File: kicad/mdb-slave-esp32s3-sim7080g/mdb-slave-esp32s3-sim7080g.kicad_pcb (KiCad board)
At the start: 2 copper layers, 65 x 40 mm, 82 parts, among them J1 USB_C_Receptacle_USB2.0_16P, J2 JAE_SIM_Card_SF72S006, J3 Conn_01x03_Pin, J4 Conn_Coaxial, J5 Conn_Coaxial, J6 MDB_Connector, J7 Conn_01x03_Pin, J8 Conn_01x04_Pin, Q1 MMBT3904, Q2 MMBT3904, Q3 MMBT3904, Q4 MMBT3904, Q5 MMBT3904, Q6 MMBT3904, Q7 MMBT3904, SW1 SW_Push, U1 ESP32-S3FH4R2, U2 SIM7080G, U3 LM2594HVM-3.3, U4 TLP785, U5 TLP785, Y1 Crystal_GND24

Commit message: Routing
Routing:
- net Net-(U1-LNA_IN/RF): track 11.7 -> 0.00 mm
- net /gnss_ant: track 7.28 -> 1.70 mm
- net /rf_ant: track 4.62 -> 1.60 mm
- net Net-(J4-In): track 4.12 -> 1.70 mm
- net /io4: track 25.2 -> 25.8 mm

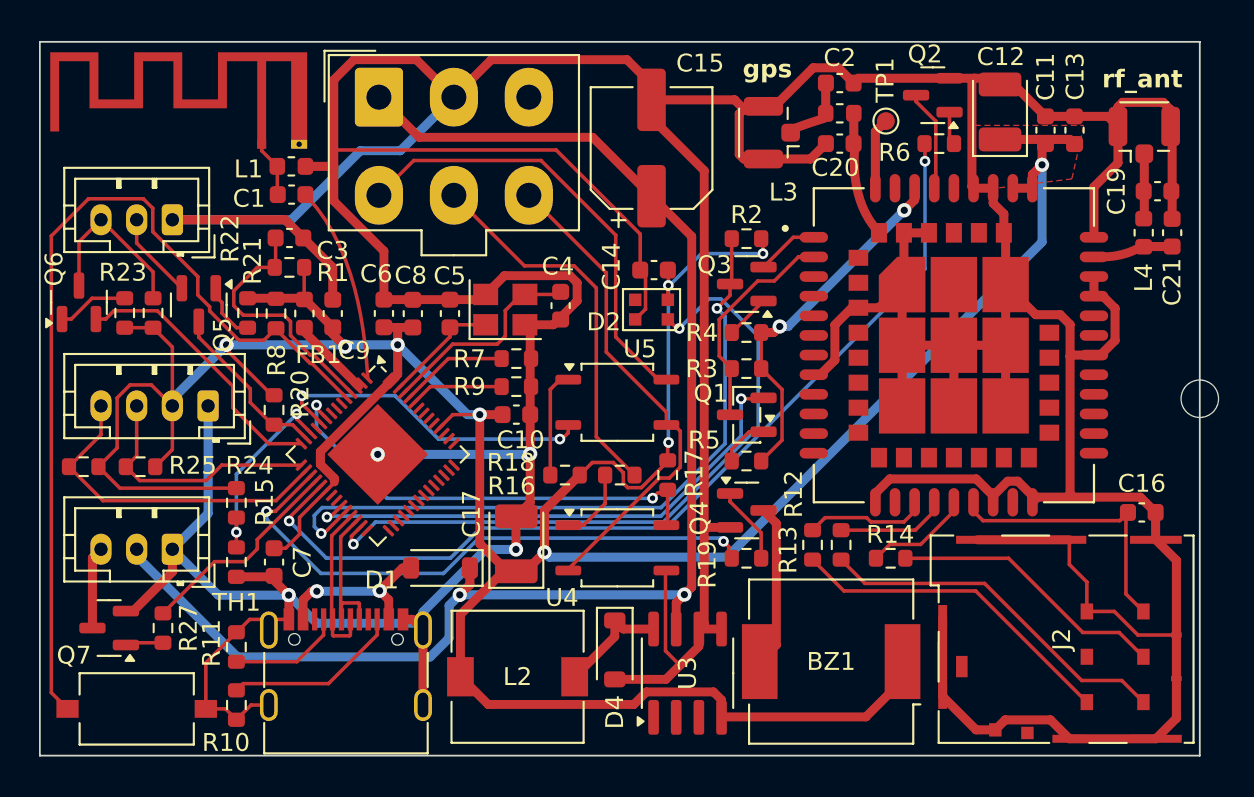
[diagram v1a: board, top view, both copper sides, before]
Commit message: Updating PCBway rules
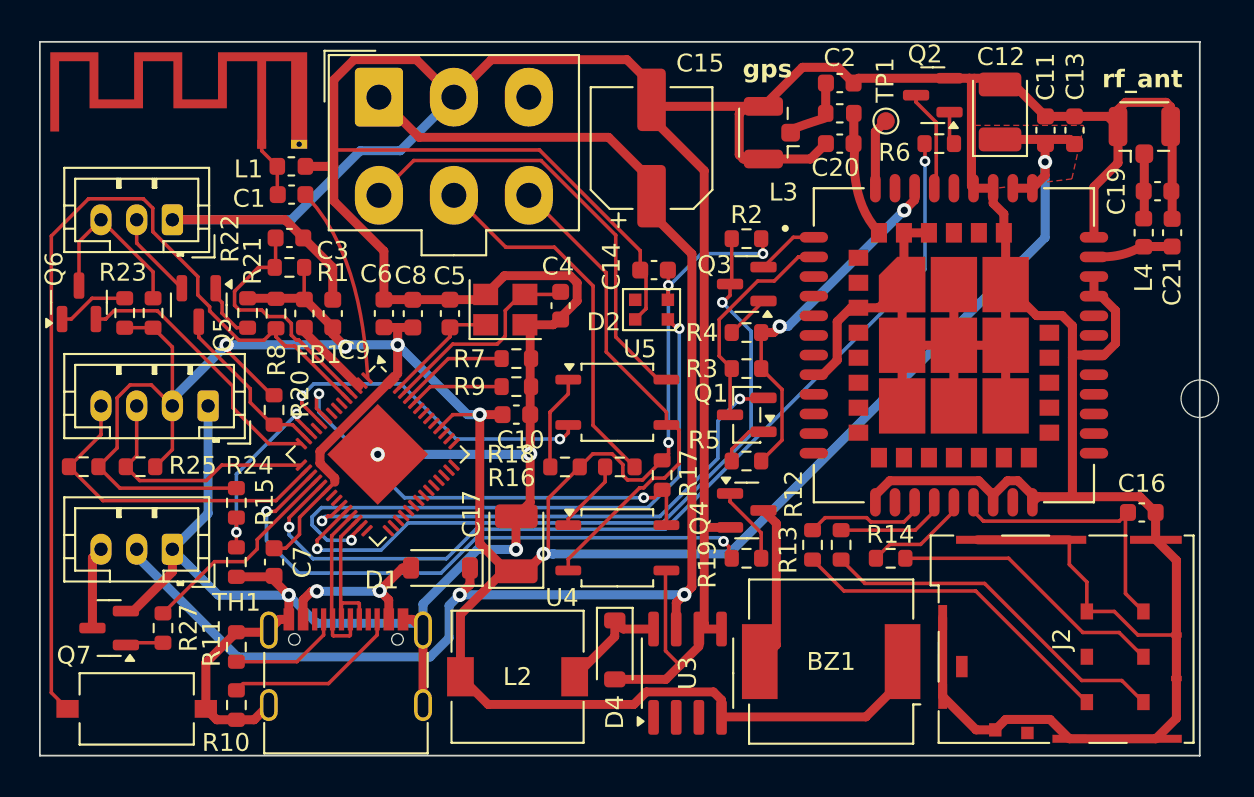
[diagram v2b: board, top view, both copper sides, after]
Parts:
- moved R16 0.46 mm to (201.0, 106.9)
- moved R18 0.46 mm to (197.9, 106.9)
- moved R17 0.31 mm to (203.4, 107.4)
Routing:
- net /io21: track 38.6 -> 34.7 mm
- net /io18: track 39.8 -> 41.7 mm
- net GND: track 427.7 -> 428.5 mm
- net /io17: track 29.5 -> 30.3 mm
- net /io12: track 32.7 -> 33.4 mm
- net Net-(R18-Pad2): track 6.03 -> 5.32 mm
- net /io5: track 18.5 -> 19.1 mm
- net /vin: track 80.8 -> 81.3 mm
- net /io14: track 53.0 -> 53.5 mm

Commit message: PCBway rules
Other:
- board text added: "d_rx"
- board text added: "d_tx"
- board text added: "gnd"
- board text added: "pulse"
- board text added: "scl"
- board text added: "sda"
- board text added: "vin"
- board text removed: "DEX"
- board text removed: "D_RX"
- board text removed: "D_TX"
- board text removed: "GND"
- board text removed: "PULSE"
- board text removed: "SCL"
- board text removed: "SDA"
- board text removed: "VIN"
- board text removed: "_i2c"
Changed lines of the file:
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@@
 		(tags "resistor")
 		(property "Reference" "R18"
-			(at 3.0375 0.7075 0)
+			(at 2.9375 0.16 0)
 			(layer "F.SilkS")
 			(effects
@@
 		(tags "capacitor")
 		(property "Reference" "C10"
-			(at 0.239166 1.42 0)
+			(at -0.250834 1.41 0)
 			(layer "F.SilkS")
 			(effects
@@
 		(tags "resistor")
 		(property "Reference" "R16"
-			(at 6.07 -0.6125 0)
+			(at 5.93 -1.16 0)
 			(layer "F.SilkS")
 			(effects
@@
 			)
 			(scale
-				(xyz 2 1 1.7)
+				(xyz 1.8 1 1.7)
 			)
 			(rotate
@@
 		)
 	)
-	(gr_text "PULSE"
-		(at 170.67 105.28 90)
+	(gr_text "pulse"
+		(at 172.589 105.75619 90)
 		(layer "B.SilkS" knockout)
 		(effects
@@
 		)
 	)
-	(gr_text "PULSE"
-		(at 172.53 105.28 90)
-		(layer "B.SilkS" knockout)
-		(effects
-			(font
-				(size 1 1)
-				(thickness 0.2)
-				(bold yes)
-			)
-			(justify left bottom mirror)
-		)
-	)
-	(gr_text "_i2c"
-		(at 170.67 98.78 90)
-		(layer "B.SilkS" knockout)
-		(effects
-			(font
-				(size 1 1)
-				(thickness 0.2)
-				(bold yes)
-			)
-			(justify left bottom mirror)
-		)
-	)
-	(gr_text "VIN"
-		(at 174.53 107.613334 90)
+	(gr_text "vin"
+		(at 174.589 107.613334 90)
 		(layer "B.SilkS" knockout)
 		(effects
@@
 	)
 	(gr_text "3v3"
-		(at 176.589 99.160952 90)
+		(at 176.589 98.970476 90)
 		(layer "B.SilkS" knockout)
 		(effects
@@
 		)
 	)
-	(gr_text "SDA"
+	(gr_text "sda"
 		(at 174.589 99.018095 90)
 		(layer "B.SilkS" knockout)
@@
 		)
 	)
-	(gr_text "GND"
-		(at 176.53 106.946667 90)
+	(gr_text "gnd"
+		(at 176.589 107.041905 90)
 		(layer "B.SilkS" knockout)
 		(effects
@@
 		)
 	)
-	(gr_text "GND"
-		(at 178.57 98.78 90)
+	(gr_text "gnd"
+		(at 178.589 98.922857 90)
 		(layer "B.SilkS" knockout)
 		(effects
@@
 		)
 	)
-	(gr_text "DEX"
-		(at 170.67 88.472381 90)
-		(layer "B.SilkS" knockout)
-		(effects
-			(font
-				(size 1 1)
-				(thickness 0.2)
-				(bold yes)
-			)
-			(justify left bottom mirror)
-		)
-	)
-	(gr_text "SCL"
-		(at 172.589 99.065714 90)
+	(gr_text "scl"
+		(at 172.589 99.446666 90)
 		(layer "B.SilkS" knockout)
 		(effects
@@
 		)
 	)
-	(gr_text "D_TX"
-		(at 172.589 87.853333 90)
+	(gr_text "d_tx"
+		(at 172.589 87.948571 90)
 		(layer "B.SilkS" knockout)
 		(effects
@@
 		)
 	)
-	(gr_text "D_RX"
-		(at 174.589 87.615238 90)
+	(gr_text "d_rx"
+		(at 174.589 87.900952 90)
 		(layer "B.SilkS" knockout)
 		(effects
@@
 		)
 	)
-	(gr_text "GND"
-		(at 176.5 88.281905 90)
+	(gr_text "gnd"
+		(at 176.589 88.281905 90)
 		(layer "B.SilkS" knockout)
 		(effects
@@
 	)
 	(zone
-		(net 3)
-		(net_name "GND")
+		(net 10)
+		(net_name "/mdb_master_transmit")
 		(layer "F.Cu")
 		(name "$teardrop_padvia$")
 		(hatch none 0.1)
-		(priority 30002)
+		(priority 30003)
 		(attr
 			(teardrop
@@
 		(polygon
 			(pts
-				(xy 190.080049 84.216496) (xy 189.726496 84.570049) (xy 190.35 86.254213) (xy 191.700707 86.190707)
-				(xy 191.485911 84.561698)
+				(xy 193.424885 93.558569) (xy 193.568569 93.414885) (xy 193.05 91.625786) (xy 191.699293 91.689293)
+				(xy 191.914088 93.318301)
 			)
 		)
 	)
 	(zone
-		(net 3)
-		(net_name "GND")
+		(net 11)
+		(net_name "/mdb_communications_common")
 		(layer "F.Cu")
 		(name "$teardrop_padvia$")
 		(hatch none 0.1)
-		(priority 30001)
+		(priority 30004)
 		(attr
 			(teardrop
@@
 		(polygon
 			(pts
-				(xy 193.673504 84.570049) (xy 193.319951 84.216496) (xy 191.914088 84.561698) (xy 191.699293 86.190707)
-				(xy 193.05 86.254214)
+				(xy 197.626017 93.557438) (xy 197.767438 93.416017) (xy 197.25 91.625786) (xy 195.899293 91.689293)
+				(xy 196.114087 93.318301)
 			)
 		)
 	)
 	(zone
-		(net 12)
-		(net_name "/mdb_master_receive")
+		(net 7)
+		(net_name "/vin")
 		(layer "F.Cu")
 		(name "$teardrop_padvia$")
 		(hatch none 0.1)
-		(priority 30005)
+		(priority 30000)
 		(attr
 			(teardrop
@@
 		(polygon
 			(pts
-				(xy 189.367438 89.963983) (xy 189.226017 89.822562) (xy 187.714088 90.061698) (xy 187.499293 91.690707)
-				(xy 188.85 91.754214)
+				(xy 189.38033 88.423883) (xy 189.733883 88.07033) (xy 188.849999 86.125786) (xy 187.499293 86.189293)
+				(xy 187.735785 87.839999)
 			)
 		)
 	)
 	(zone
-		(net 11)
-		(net_name "/mdb_communications_common")
+		(net 3)
+		(net_name "GND")
 		(layer "F.Cu")
 		(name "$teardrop_padvia$")
 		(hatch none 0.1)
-		(priority 30004)
+		(priority 30002)
 		(attr
 			(teardrop
@@
 		(polygon
 			(pts
-				(xy 197.626017 93.557438) (xy 197.767438 93.416017) (xy 197.25 91.625786) (xy 195.899293 91.689293)
-				(xy 196.114087 93.318301)
+				(xy 190.080049 84.216496) (xy 189.726496 84.570049) (xy 190.35 86.254213) (xy 191.700707 86.190707)
+				(xy 191.485911 84.561698)
 			)
 		)
 	)
 	(zone
-		(net 10)
-		(net_name "/mdb_master_transmit")
+		(net 12)
+		(net_name "/mdb_master_receive")
 		(layer "F.Cu")
 		(name "$teardrop_padvia$")
 		(hatch none 0.1)
-		(priority 30003)
+		(priority 30005)
 		(attr
 			(teardrop
@@
 		(polygon
 			(pts
-				(xy 193.424885 93.558569) (xy 193.568569 93.414885) (xy 193.05 91.625786) (xy 191.699293 91.689293)
-				(xy 191.914088 93.318301)
+				(xy 189.367438 89.963983) (xy 189.226017 89.822562) (xy 187.714088 90.061698) (xy 187.499293 91.690707)
+				(xy 188.85 91.754214)
 			)
 		)
 	)
 	(zone
-		(net 7)
-		(net_name "/vin")
+		(net 3)
+		(net_name "GND")
 		(layer "F.Cu")
 		(name "$teardrop_padvia$")
 		(hatch none 0.1)
-		(priority 30000)
+		(priority 30001)
 		(attr
 			(teardrop
@@
 		(polygon
 			(pts
-				(xy 189.38033 88.423883) (xy 189.733883 88.07033) (xy 188.849999 86.125786) (xy 187.499293 86.189293)
-				(xy 187.735785 87.839999)
+				(xy 193.673504 84.570049) (xy 193.319951 84.216496) (xy 191.914088 84.561698) (xy 191.699293 86.190707)
+				(xy 193.05 86.254214)
 			)
 		)

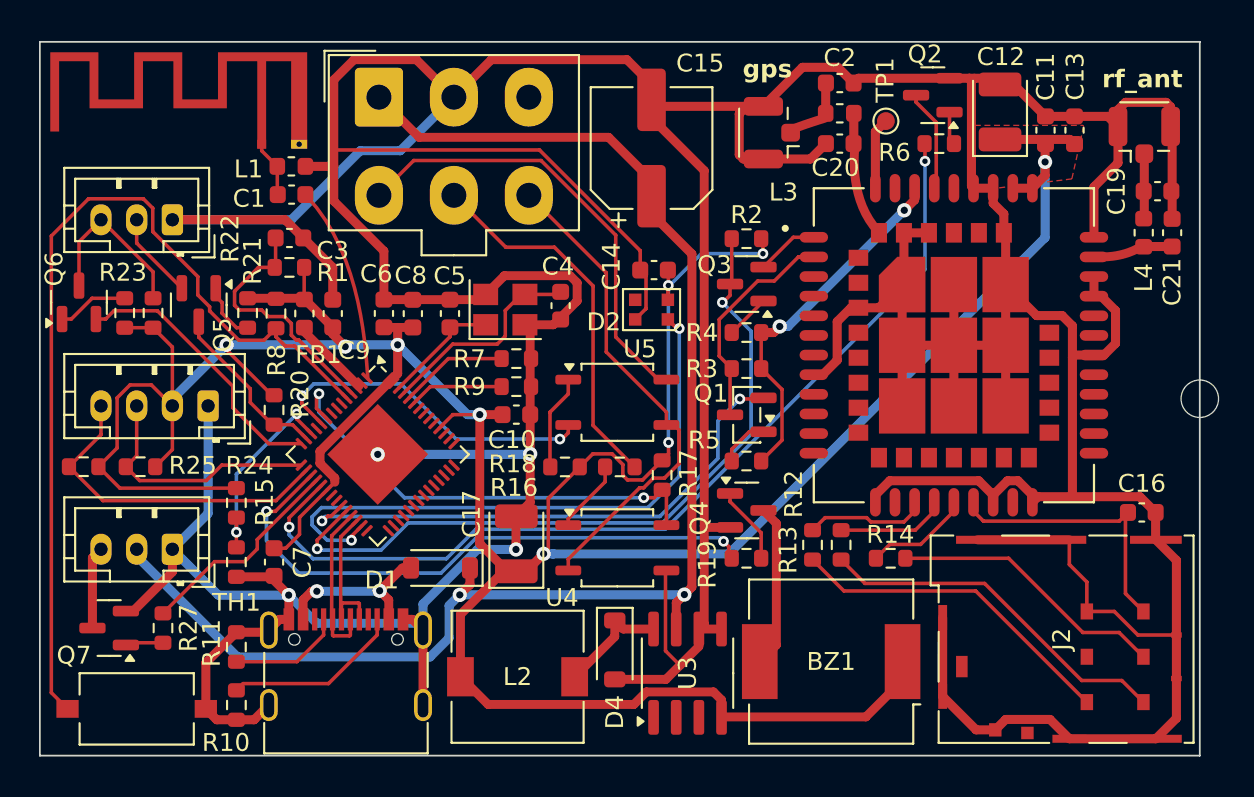
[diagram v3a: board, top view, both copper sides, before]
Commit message: Feat/gnd plane routing (#50)
Implement GND plane routing and optimize return paths
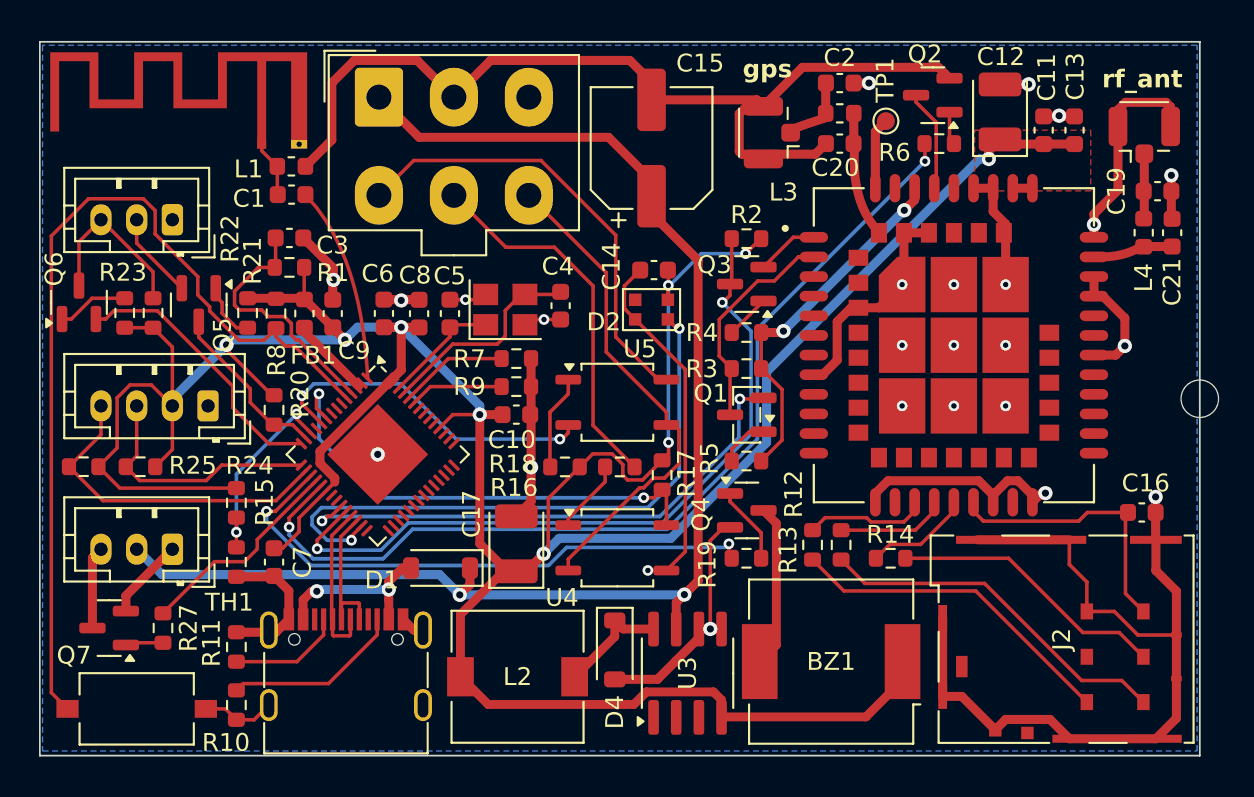
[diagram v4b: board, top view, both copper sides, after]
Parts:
- moved REF** 4.86 mm to (206.5, 106.4)
- moved C8 0.35 mm to (189.8, 98.3)
- moved C11 0.10 mm to (224.8, 88.0)
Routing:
- net GND: track 428.5 -> 231.5 mm, vias 4 -> 25
- net +3V3: track 208.3 -> 204.0 mm
- net /vin: track 81.3 -> 77.4 mm
- net /io12: track 33.4 -> 32.2 mm
- net /io4: track 26.2 -> 27.1 mm
- added copper zone on B.Cu, net GND
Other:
- board text added: "commit: xxxxxxx"

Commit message: Changing silk label text
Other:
- board text added: "rx"
- board text added: "tx"
- board text removed: "d_rx"
- board text removed: "d_tx"
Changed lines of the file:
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@@
 		)
 	)
-	(gr_text "d_tx"
-		(at 172.589 87.948571 90)
+	(gr_text "tx"
+		(at 172.589 89.615238 90)
 		(layer "B.SilkS" knockout)
 		(effects
@@
 		)
 	)
-	(gr_text "d_rx"
-		(at 174.589 87.900952 90)
+	(gr_text "rx"
+		(at 174.589 89.567619 90)
 		(layer "B.SilkS" knockout)
 		(effects

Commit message: routing...
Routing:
- net +3V3: track 204.0 -> 222.1 mm, vias 9 -> 7
- net GND: track 231.5 -> 230.5 mm

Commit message: routing pcb
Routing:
- net GND: track 230.5 -> 218.6 mm, vias 25 -> 26
- net /vin: track 77.7 -> 76.9 mm
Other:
- board text added: "commit xxxxxxx"
- board text removed: "commit: xxxxxxx"
